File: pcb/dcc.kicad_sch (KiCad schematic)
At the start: 52 parts, among them U10 LM339, U11 LM339, U4 L78L05_SOT89, U5 L79L05_SOT89, U6 LM339, U7 LM339, U8 LM339, U9 4052

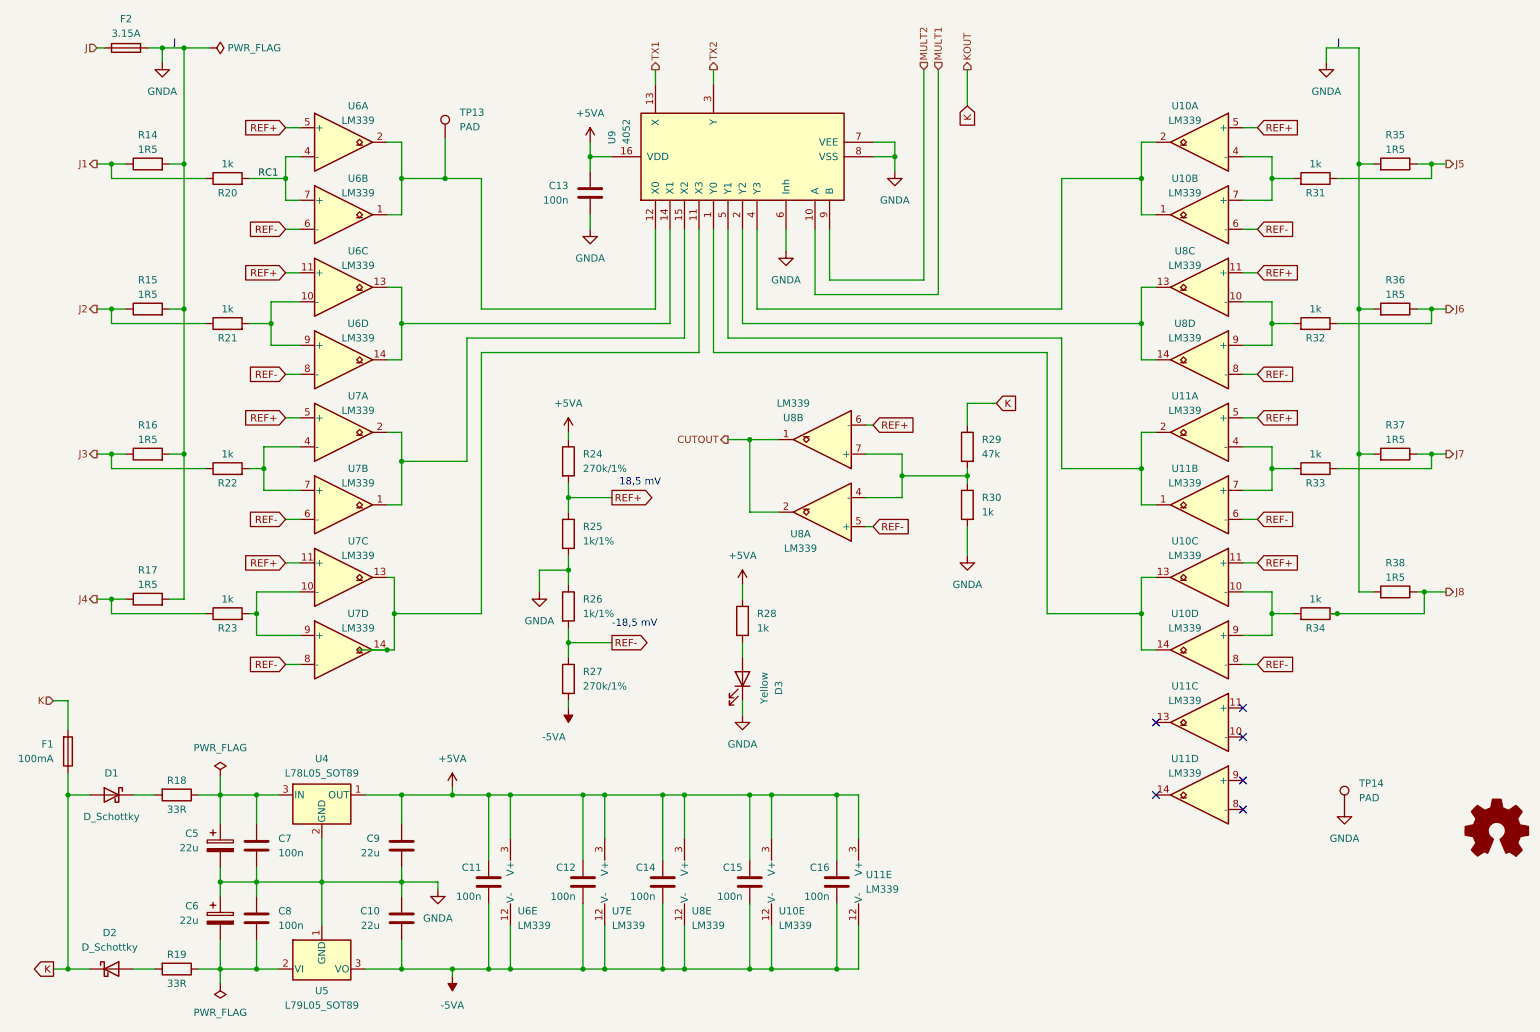
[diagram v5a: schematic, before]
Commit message: Added Sch.diodes, text editing..
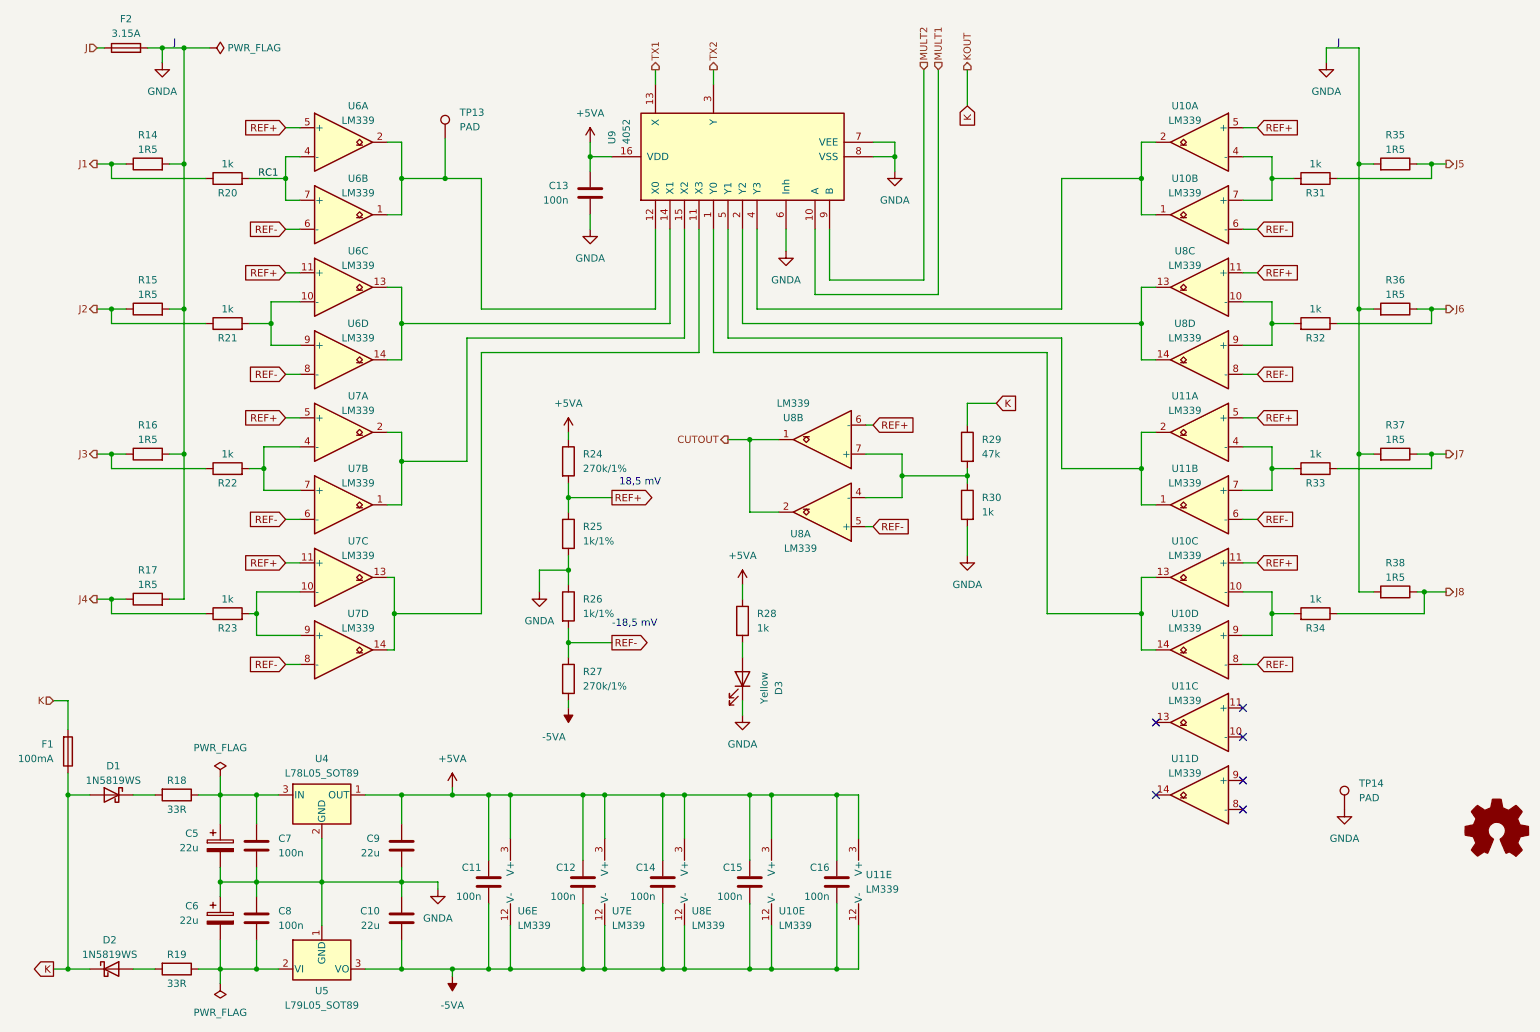
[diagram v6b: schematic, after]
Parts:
- removed D1, D2: D_Schottky, symbol Device:D_Schottky
- added D1, D2: 1N5819WS, Diode_SMD:D_SOD-123, symbol Diode:1N5819WS
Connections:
- net K: now also D1.2 (A), D2.1 (K)
- net at R19.2: now also D2.2 (A)
- net at R18.2: now also D1.1 (K)
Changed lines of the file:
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@@
   (junction (at 33.02 41.91) (diameter 0) (color 0 0 0 0)
   )
-  (junction (at 81.28 127) (diameter 0) (color 0 0 0 0)
-  )
   (junction (at 113.03 125.73) (diameter 0) (color 0 0 0 0)
   )
@@
   (junction (at 144.78 182.88) (diameter 0) (color 0 0 0 0)
   )
-  (junction (at 247.65 120.65) (diameter 0) (color 0 0 0 0)
-  )
   (junction (at 170.18 40.64) (diameter 0) (color 0 0 0 0)
   )
@@
     (stroke (width 0) (type default))
   )
+  (wire (pts (xy 81.28 127) (xy 82.55 127))
+    (stroke (width 0) (type default))
+  )
   (wire (pts (xy 83.82 38.1) (xy 81.28 38.1))
     (stroke (width 0) (type default))
@@
     (stroke (width 0) (type default))
   )
-  (wire (pts (xy 81.28 127) (xy 82.55 127))
-    (stroke (width 0) (type default))
-  )
   (wire (pts (xy 236.22 66.04) (xy 236.22 69.85))
     (stroke (width 0) (type default))
@@
     (stroke (width 0) (type default))
   )
-  (wire (pts (xy 76.2 127) (xy 81.28 127))
-    (stroke (width 0) (type default))
-  )
   (wire (pts (xy 83.82 93.98) (xy 95.25 93.98))
     (stroke (width 0) (type default))
@@
     (stroke (width 0) (type default))
   )
-  (wire (pts (xy 247.65 120.65) (xy 262.89 120.65))
-    (stroke (width 0) (type default))
-  )
   (wire (pts (xy 83.82 167.64) (xy 83.82 170.18))
     (stroke (width 0) (type default))
@@
     (stroke (width 0) (type default))
   )
-  (wire (pts (xy 246.38 120.65) (xy 247.65 120.65))
-    (stroke (width 0) (type default))
-  )
   (wire (pts (xy 156.21 64.77) (xy 177.8 64.77))
     (stroke (width 0) (type default))
@@
     (stroke (width 0) (type default))
   )
+  (wire (pts (xy 247.65 120.65) (xy 262.89 120.65))
+    (stroke (width 0) (type default))
+  )
   (wire (pts (xy 63.5 111.76) (xy 66.04 111.76))
     (stroke (width 0) (type default))
@@
     )
   )
+  (symbol (lib_id "Diode:1N5819WS") (at 33.02 182.88 0) (unit 1)
+    (in_bom yes) (on_board yes) (dnp no) (fields_autoplaced)
+    (property "Reference" "D2" (at 32.7025 177.8 0)
+      (effects (font (size 1.27 1.27)))
+    )
+    (property "Value" "1N5819WS" (at 32.7025 180.34 0)
+      (effects (font (size 1.27 1.27)))
+    )
+    (property "Footprint" "Diode_SMD:D_SOD-123" (at 33.02 187.325 0)
+      (effects (font (size 1.27 1.27)) hide)
+    )
+    (property "Datasheet" "https://datasheet.lcsc.com/lcsc/2204281430_Guangdong-Hottech-1N5819WS_C191023.pdf" (at 33.02 182.88 0)
+      (effects (font (size 1.27 1.27)) hide)
+    )
+    (pin "1")
+    (pin "2")
+    (instances
+      (project "railcomdet"
+        (path "/3e59d29f-2657-4552-9290-3c54fadfdf63/e5256faa-a48e-4175-bec4-bd0fa3c5f991"
+          (reference "D2") (unit 1)
+        )
+      )
+    )
+  )
   (symbol (lib_id "Comparator:LM339") (at 223.52 76.2 0) (mirror y) (unit 4)
     (in_bom yes) (on_board yes) (dnp no)
@@
     )
   )
+  (symbol (lib_id "Diode:1N5819WS") (at 33.02 152.4 0) (mirror y) (unit 1)
+    (in_bom yes) (on_board yes) (dnp no)
+    (property "Reference" "D1" (at 33.3375 147.32 0)
+      (effects (font (size 1.27 1.27)))
+    )
+    (property "Value" "1N5819WS" (at 33.3375 149.86 0)
+      (effects (font (size 1.27 1.27)))
+    )
+    (property "Footprint" "Diode_SMD:D_SOD-123" (at 33.02 156.845 0)
+      (effects (font (size 1.27 1.27)) hide)
+    )
+    (property "Datasheet" "https://datasheet.lcsc.com/lcsc/2204281430_Guangdong-Hottech-1N5819WS_C191023.pdf" (at 33.02 152.4 0)
+      (effects (font (size 1.27 1.27)) hide)
+    )
+    (pin "1")
+    (pin "2")
+    (instances
+      (project "railcomdet"
+        (path "/3e59d29f-2657-4552-9290-3c54fadfdf63/e5256faa-a48e-4175-bec4-bd0fa3c5f991"
+          (reference "D1") (unit 1)
+        )
+      )
+    )
+  )
   (symbol (lib_id "Device:R") (at 39.37 92.71 90) (unit 1)
     (in_bom yes) (on_board yes) (dnp no)
@@
     )
   )
-  (symbol (lib_id "Device:D_Schottky") (at 33.02 182.88 0) (unit 1)
-    (in_bom yes) (on_board yes) (dnp no)
-    (property "Reference" "D2" (at 32.7025 176.53 0)
-      (effects (font (size 1.27 1.27)))
-    )
-    (property "Value" "D_Schottky" (at 32.7025 179.07 0)
-      (effects (font (size 1.27 1.27)))
-    )
-    (property "Footprint" "" (at 33.02 182.88 0)
-      (effects (font (size 1.27 1.27)) hide)
-    )
-    (property "Datasheet" "~" (at 33.02 182.88 0)
-      (effects (font (size 1.27 1.27)) hide)
-    )
-    (pin "1")
-    (pin "2")
-    (instances
-      (project "railcomdet"
-        (path "/3e59d29f-2657-4552-9290-3c54fadfdf63/e5256faa-a48e-4175-bec4-bd0fa3c5f991"
-          (reference "D2") (unit 1)
-        )
-      )
-    )
-  )
   (symbol (lib_id "Comparator:LM339") (at 157.48 102.87 180) (unit 1)
     (in_bom yes) (on_board yes) (dnp no)
@@
         )
       )
-    )
-  )
-  (symbol (lib_id "Device:D_Schottky") (at 33.02 152.4 0) (mirror y) (unit 1)
-    (in_bom yes) (on_board yes) (dnp no)
-    (property "Reference" "D1" (at 33.02 148.59 0)
-      (effects (font (size 1.27 1.27)))
-    )
-    (property "Value" "D_Schottky" (at 33.02 156.21 0)
-      (effects (font (size 1.27 1.27)))
-    )
-    (property "Footprint" "" (at 33.02 152.4 0)
-      (effects (font (size 1.27 1.27)) hide)
-    )
-    (property "Datasheet" "~" (at 33.02 152.4 0)
-      (effects (font (size 1.27 1.27)) hide)
-    )
-    (pin "1")
-    (pin "2")
-    (instances
-      (project "railcomdet"
-        (path "/3e59d29f-2657-4552-9290-3c54fadfdf63/e5256faa-a48e-4175-bec4-bd0fa3c5f991"
-          (reference "D1") (unit 1)
-        )
-      )

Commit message: Added Schottky in DCC part and fuse footprint.
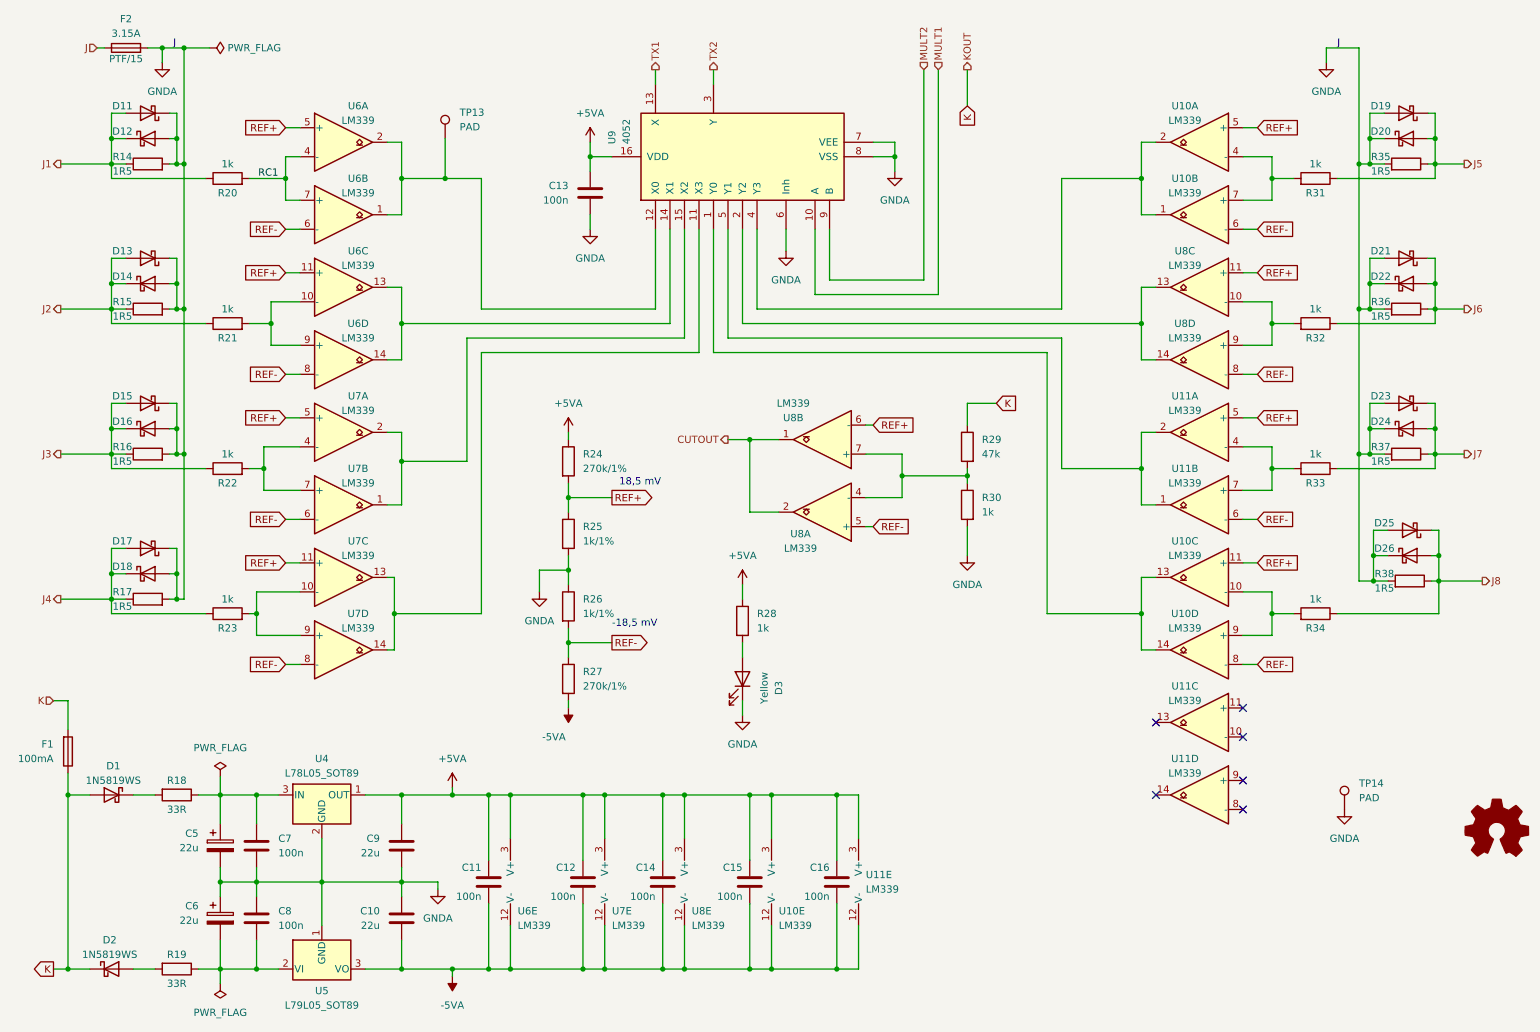
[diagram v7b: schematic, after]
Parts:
- added D11, D12, D13, D14, D15, D16, D17, D18, D19, D20, D21, D22, D23, D24, D25, D26: D_Schottky, symbol Device:D_Schottky
- F2: footprint (none) -> Fuse:Fuseholder_Cylinder-5x20mm_Stelvio-Kontek_PTF78_Horizontal_Open; atribut (none) -> PTF/15
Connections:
- net GNDA: now also D11.1 (K), D12.2 (A), D13.1 (K), D14.2 (A), D15.1 (K), D16.2 (A), D17.1 (K), D18.2 (A), D19.2 (A), D20.1 (K), D21.2 (A), D22.1 (K), D23.2 (A), D24.1 (K), D25.2 (A), D26.1 (K)
- net J1: now also D11.2 (A), D12.1 (K)
- net J2: now also D13.2 (A), D14.1 (K)
- net J3: now also D15.2 (A), D16.1 (K)
- net J4: now also D17.2 (A), D18.1 (K)
- net J5: now also D19.1 (K), D20.2 (A)
- net J6: now also D21.1 (K), D22.2 (A)
- net J7: now also D23.1 (K), D24.2 (A)
- net J8: now also D25.1 (K), D26.2 (A)
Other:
- moved on the sheet: R35, R36, R37, R38
